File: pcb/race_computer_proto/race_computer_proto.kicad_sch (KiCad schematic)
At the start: 12 parts, among them U1 Teensy4.0, U3 SN74LVC245APW

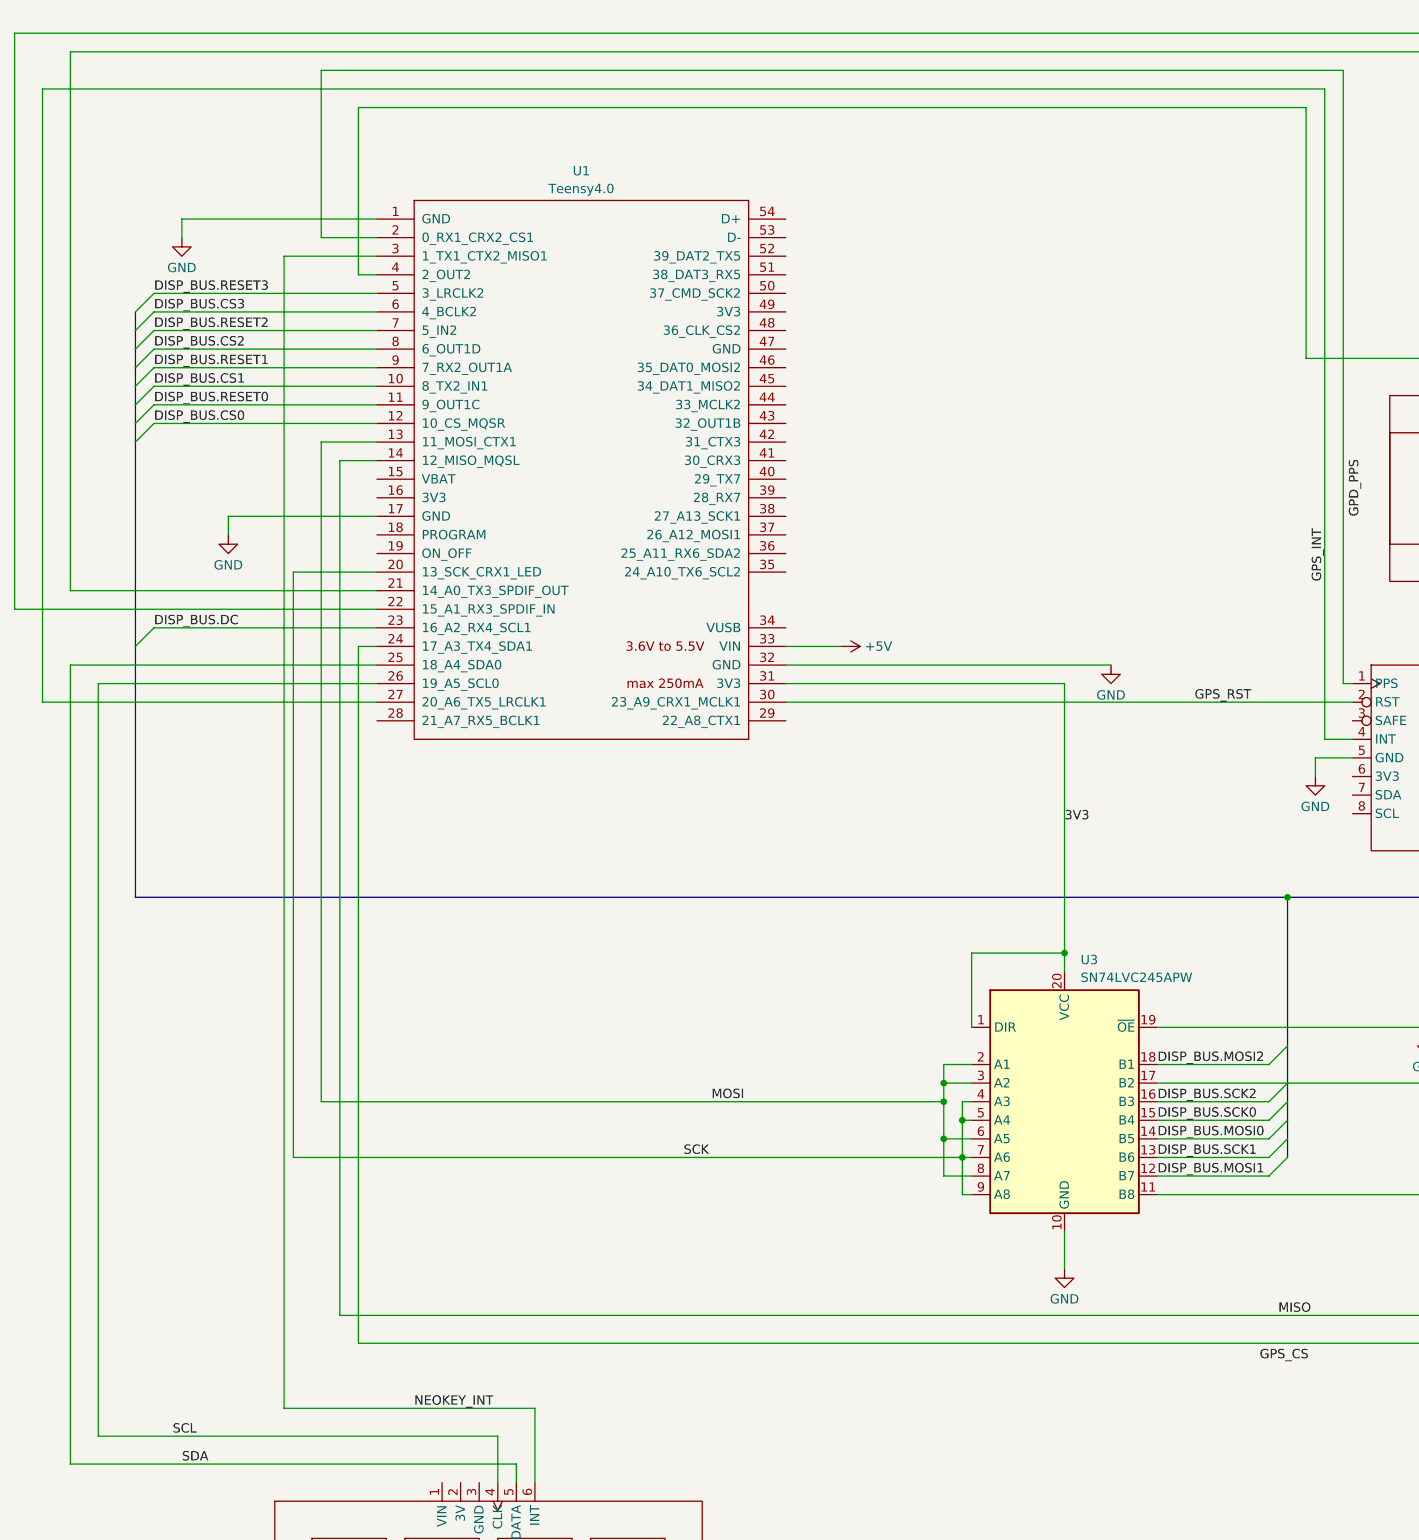
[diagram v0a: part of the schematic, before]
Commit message: Add missing chip select for LED display. Reorder OLED control pins so that GPS PPS signal is on Teensy pin 9. PPS must be on a pin that can be used as a timer input. Re-route PCB with above changes.
TODO:  Correct power board pinout (reversed).  Correct OLED connector pinour (mirrored).

Switch to callbacks for most GPS packet updates.
Displays now show: time delta, speed delta, distance remaining, distance traveled, speed, and average speed.
Enabled odometer and switched average speed calc to be based on the odometer.
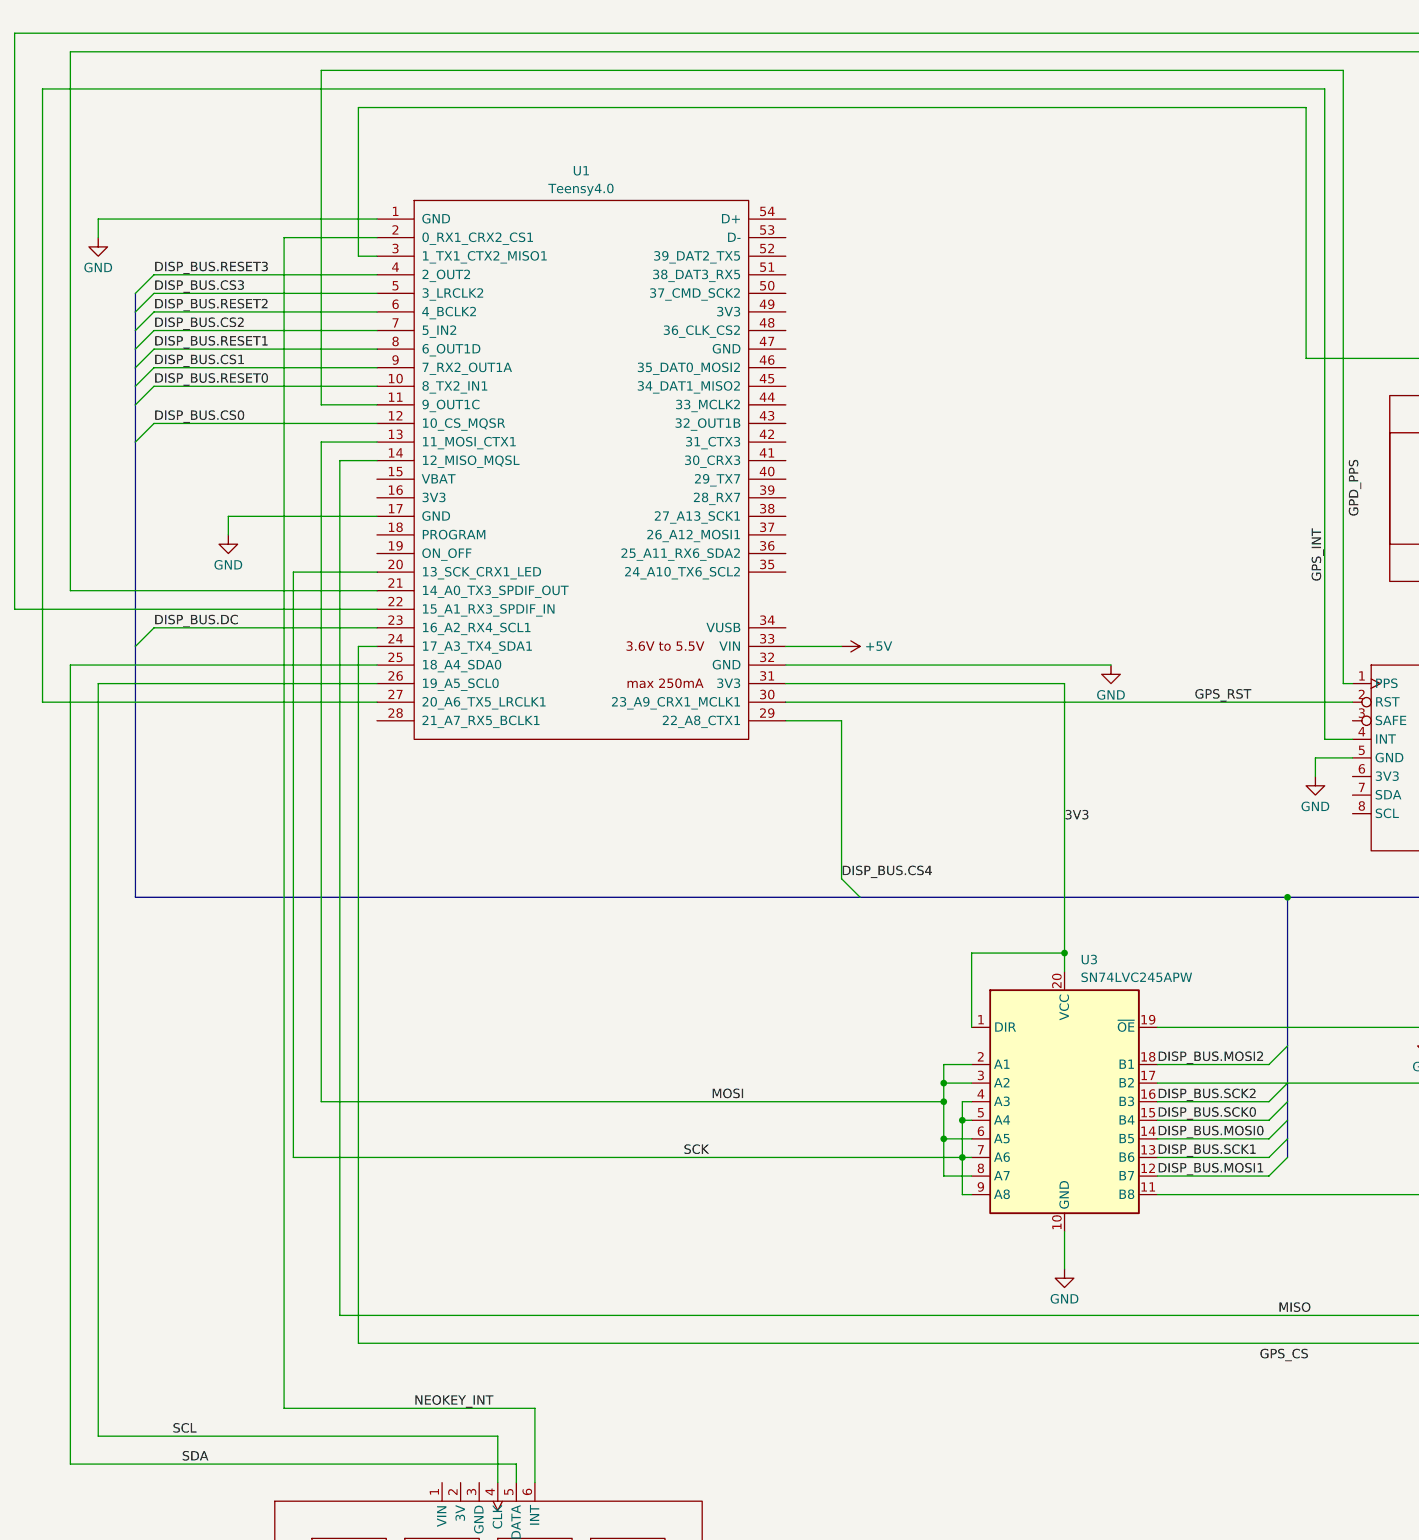
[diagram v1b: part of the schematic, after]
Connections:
- net DISP_BUS.CS1: now also U1.9 (7_RX2_OUT1A); no longer U1.10 (8_TX2_IN1)
- net DISP_BUS.CS2: now also U1.7 (5_IN2); no longer U1.8 (6_OUT1D)
- net DISP_BUS.CS3: now also U1.5 (3_LRCLK2); no longer U1.6 (4_BCLK2)
- net DISP_BUS.CS4: now also U1.29 (22_A8_CTX1)
- net DISP_BUS.RESET0: now also U1.10 (8_TX2_IN1); no longer U1.11 (9_OUT1C)
- net DISP_BUS.RESET1: now also U1.8 (6_OUT1D); no longer U1.9 (7_RX2_OUT1A)
- net DISP_BUS.RESET2: now also U1.6 (4_BCLK2); no longer U1.7 (5_IN2)
- net DISP_BUS.RESET3: now also U1.4 (2_OUT2); no longer U1.5 (3_LRCLK2)
- net NEOKEY_INT: now also U1.2 (0_RX1_CRX2_CS1); no longer U1.3 (1_TX1_CTX2_MISO1)
- net SDCARD_CS: now also U1.3 (1_TX1_CTX2_MISO1); no longer U1.4 (2_OUT2)
- net at U2.1 (PPS): now also U1.11 (9_OUT1C); no longer U1.2 (0_RX1_CRX2_CS1)

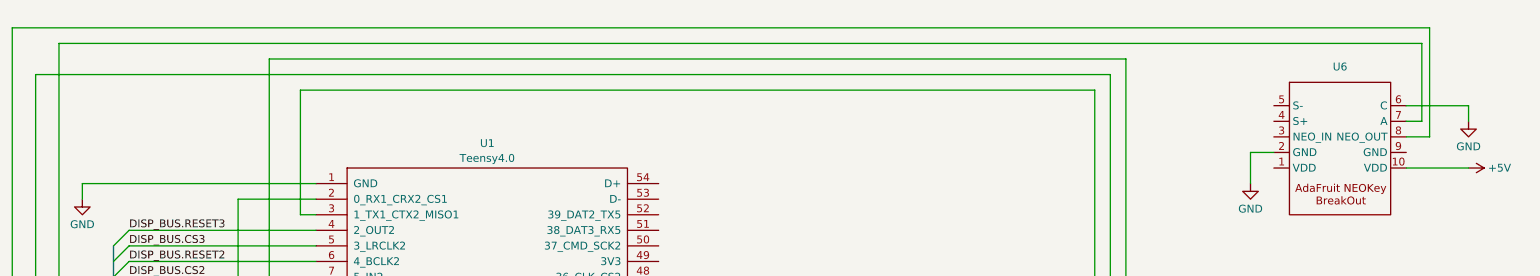
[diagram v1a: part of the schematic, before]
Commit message: Convert timer callback list to an object based event list to allow more flexible use. Add bitmaps for boot splash. Completed prototype case model. Corrected neokey breakout connections on schematic and PCB.  Removed only via from PCB.
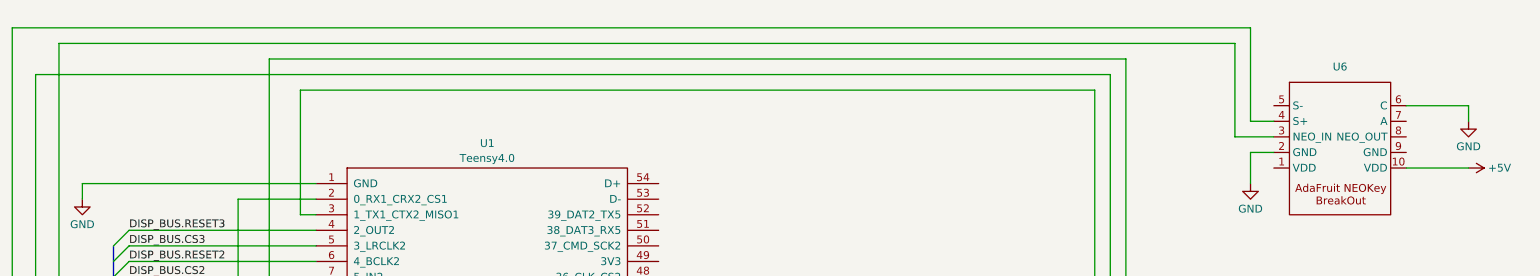
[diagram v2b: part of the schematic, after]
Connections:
- net at U1.21 (14_A0_TX3_SPDIF_OUT): now also U6.3 (NEO_IN); no longer U6.7 (A)
- net at U1.22 (15_A1_RX3_SPDIF_IN): now also U6.4 (S+); no longer U6.8 (NEO_OUT)
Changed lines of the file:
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@@
-	(wire
-		(pts
-			(xy 254 35.56) (xy 254 17.78)
-		)
-		(stroke
-			(width 0)
-			(type default)
-		)
-	)
 	(wire
 		(pts
@@
 	(wire
 		(pts
-			(xy 22.86 17.78) (xy 254 17.78)
+			(xy 22.86 17.78) (xy 224.79 17.78)
+		)
+		(stroke
+			(width 0)
+			(type default)
+		)
+	)
+	(wire
+		(pts
+			(xy 222.25 35.56) (xy 228.6 35.56)
 		)
 		(stroke
@@
 	(wire
 		(pts
-			(xy 250.19 33.02) (xy 252.73 33.02)
-		)
-		(stroke
-			(width 0)
-			(type default)
-		)
-	)
-	(wire
-		(pts
 			(xy 307.34 20.32) (xy 309.88 20.32)
 		)
@@
 	(wire
 		(pts
-			(xy 252.73 33.02) (xy 252.73 20.32)
-		)
-		(stroke
-			(width 0)
-			(type default)
-		)
-	)
-	(wire
-		(pts
 			(xy 199.39 27.94) (xy 199.39 62.23)
 		)
@@
 	(wire
 		(pts
+			(xy 224.79 33.02) (xy 228.6 33.02)
+		)
+		(stroke
+			(width 0)
+			(type default)
+		)
+	)
+	(wire
+		(pts
 			(xy 289.56 149.86) (xy 309.88 149.86)
 		)
@@
 	(wire
 		(pts
-			(xy 30.48 20.32) (xy 252.73 20.32)
+			(xy 30.48 20.32) (xy 222.25 20.32)
 		)
 		(stroke
@@
 	(wire
 		(pts
-			(xy 250.19 35.56) (xy 254 35.56)
-		)
-		(stroke
-			(width 0)
-			(type default)
-		)
-	)
-	(wire
-		(pts
 			(xy 308.61 48.26) (xy 309.88 48.26)
 		)
@@
 		)
 	)
+	(wire
+		(pts
+			(xy 222.25 20.32) (xy 222.25 35.56)
+		)
+		(stroke
+			(width 0)
+			(type default)
+		)
+	)
 	(bus
 		(pts
@@
 		)
 		(stroke
+			(width 0)
+			(type default)
+		)
+	)
+	(wire
+		(pts
+			(xy 224.79 17.78) (xy 224.79 33.02)
+		)
+		(stroke
